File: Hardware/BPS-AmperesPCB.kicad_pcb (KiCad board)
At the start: 2 copper layers, 70 x 60 mm, 45 parts, among them J1 Conn_01x04, J2 PeripheralCANConnector, J3 PeripheralCANConnector, U1 PeripheralSOM, U2 INA145UA/2K5, U3 AMC1300BDWV, U4 RO-123.3S_HP

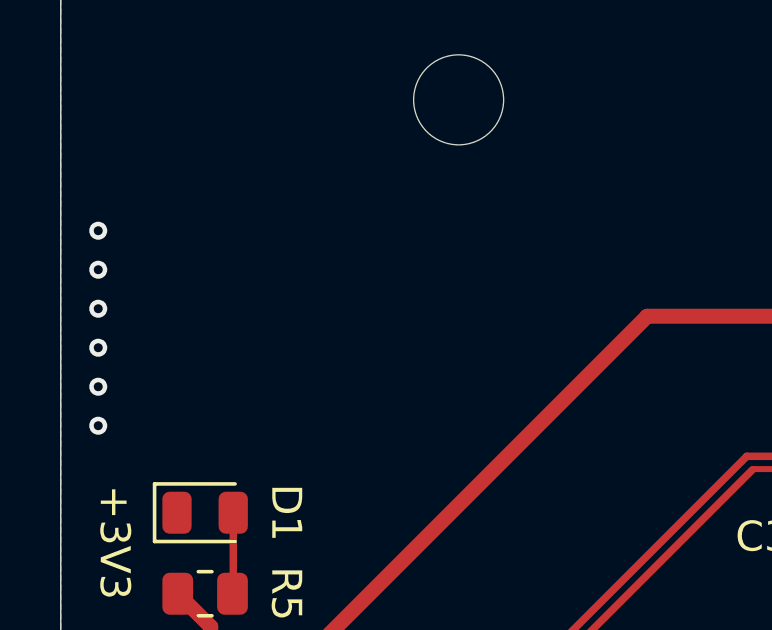
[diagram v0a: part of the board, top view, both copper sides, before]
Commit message: new isolated amp, filter stage; need to select values
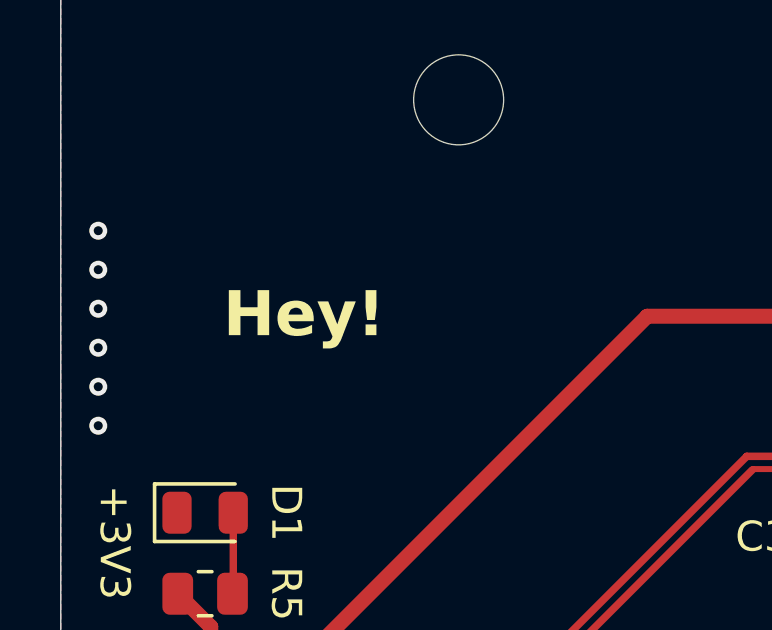
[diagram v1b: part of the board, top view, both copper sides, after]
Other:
- board text added: "Hey!"
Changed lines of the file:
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@@
 			(psa4output no)
 			(plot_black_and_white yes)
-			(plotinvisibletext no)
 			(sketchpadsonfab no)
 			(plotpadnumbers no)
@@
 			)
 			(justify left bottom)
+		)
+	)
+	(gr_text "Hey!"
+		(at 73.914 54.864 0)
+		(layer "F.SilkS" knockout)
+		(effects
+			(font
+				(size 1.5 1.5)
+				(thickness 0.3)
+				(bold yes)
+			)
+			(justify left bottom)
